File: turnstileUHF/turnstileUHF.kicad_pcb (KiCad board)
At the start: 2 copper layers, 98 x 98 mm, 49 parts, among them Q1 2N7002, Q2 2N7002, Q3 2N7002, Q4 2N7002, Q5 AO3401A, Q6 AO3401A, Q7 AO3401A, Q8 2N7002, SW1 SW_DIP_x04

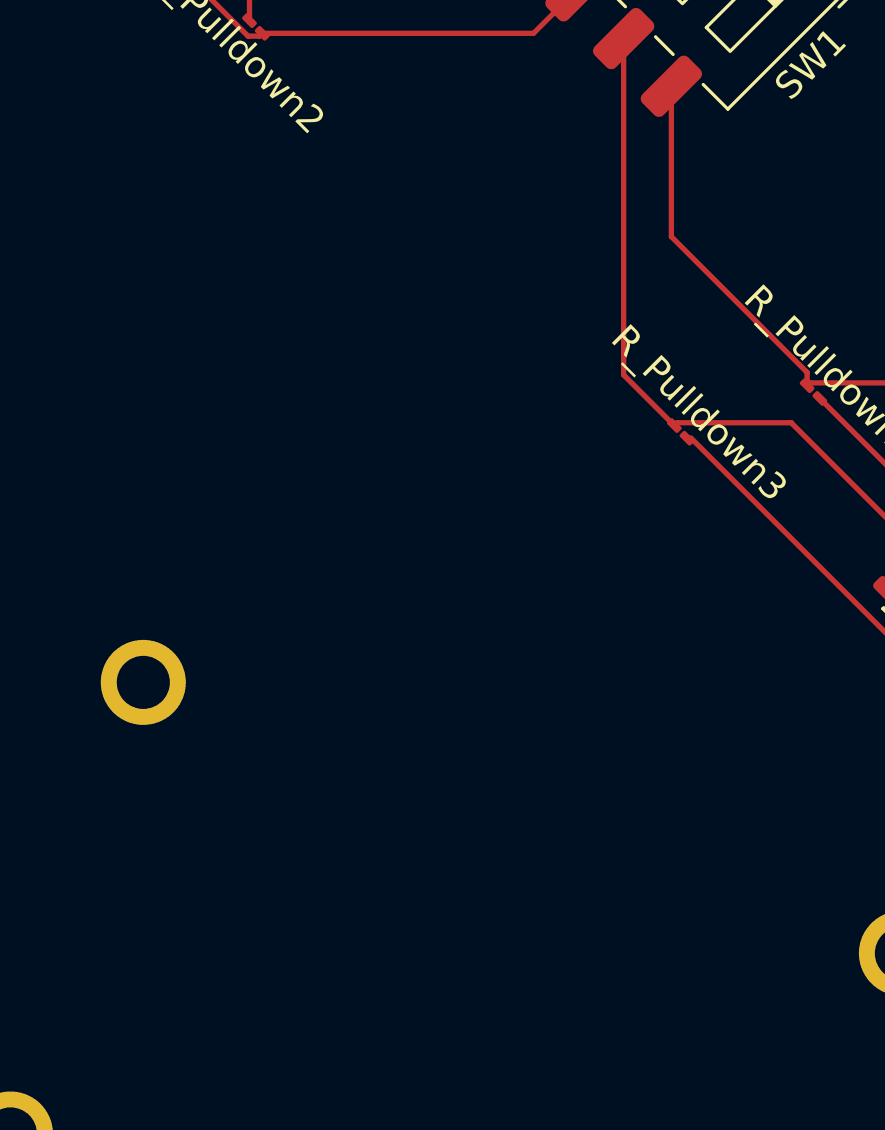
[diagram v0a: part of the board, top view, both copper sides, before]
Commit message: added trace antennas with coax links
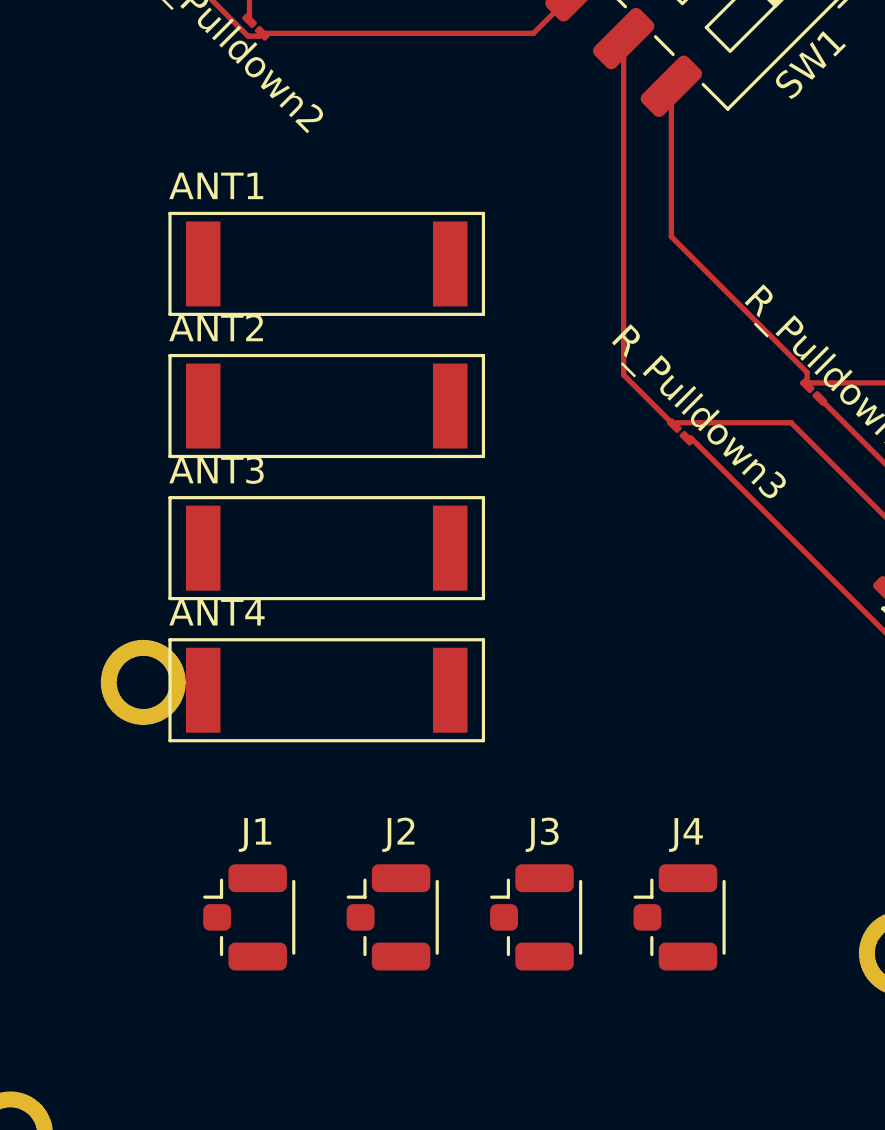
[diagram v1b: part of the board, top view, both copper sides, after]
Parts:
- added ANT1: Antenna, RF_Antenna:Coilcraft_MA5532-AE_RFID, F.Cu at (176.7, 124.4)
- added ANT2: Antenna, RF_Antenna:Coilcraft_MA5532-AE_RFID, F.Cu at (176.7, 129.8)
- added ANT3: Antenna, RF_Antenna:Coilcraft_MA5532-AE_RFID, F.Cu at (176.7, 135.1)
- added ANT4: Antenna, RF_Antenna:Coilcraft_MA5532-AE_RFID, F.Cu at (176.7, 140.5)
- added J1: Conn_Coaxial, Connector_Coaxial:U.FL_Hirose_U.FL-R-SMT-1_Vertical, F.Cu at (174.1, 149.0)
- added J2: Conn_Coaxial, Connector_Coaxial:U.FL_Hirose_U.FL-R-SMT-1_Vertical, F.Cu at (179.5, 149.0)
- added J3: Conn_Coaxial, Connector_Coaxial:U.FL_Hirose_U.FL-R-SMT-1_Vertical, F.Cu at (184.9, 149.0)
- added J4: Conn_Coaxial, Connector_Coaxial:U.FL_Hirose_U.FL-R-SMT-1_Vertical, F.Cu at (190.3, 149.0)

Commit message: Added new 74HCT238D decoder and re-organisation of schematic
Added the 74HCT238D decoder and I also re-organised the schematic.
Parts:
- added U1: 74HCT238D, inspireFly:SOT109-1_NXP, F.Cu at (176.1, 127.4)
- moved ANT4 48.1 mm to (143.2, 106.0)
- moved ANT1 31.8 mm to (146.7, 114.0)
- moved ANT2 31.1 mm to (147.0, 120.5)
- moved ANT3 30.2 mm to (147.5, 127.5)
- moved J4 4.42 mm to (188.5, 145.0)

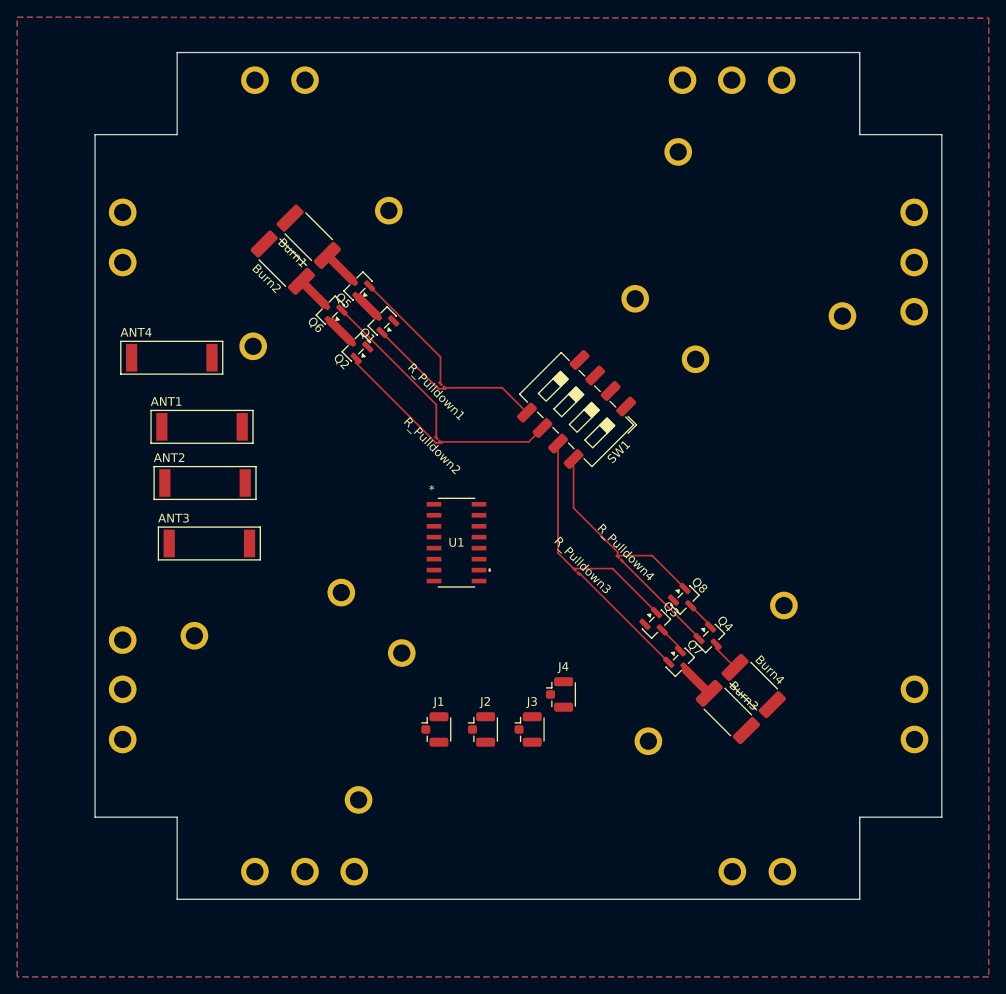
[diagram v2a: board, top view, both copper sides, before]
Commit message: Further changes made. Added SMA connector & Changed the placement of the trace antennas
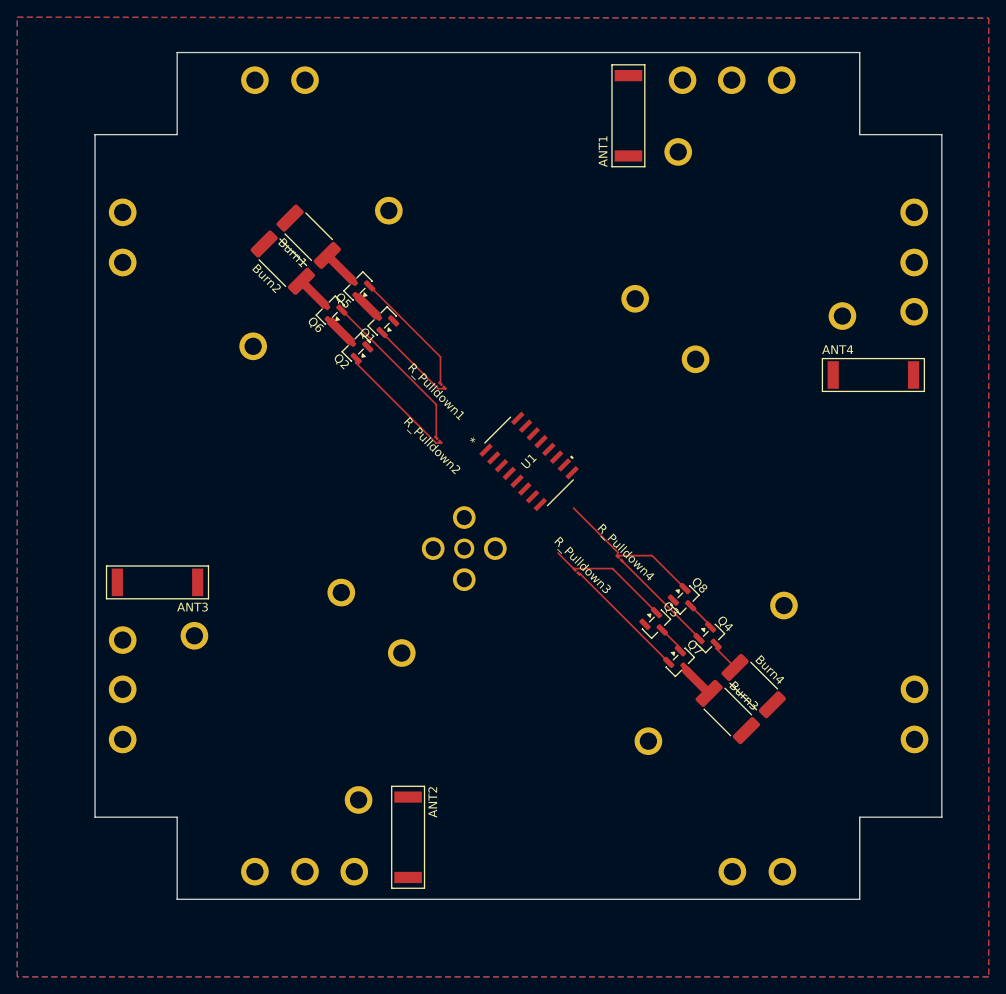
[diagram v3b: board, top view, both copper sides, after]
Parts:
- removed J1, J2, J3, J4: Conn_Coaxial, Connector_Coaxial:U.FL_Hirose_U.FL-R-SMT-1_Vertical
- removed SW1: SW_DIP_x04, Button_Switch_SMD:SW_DIP_SPSTx04_Slide_6.7x11.72mm_W8.61mm_P2.54mm_LowProfile
- added J5: RFPC-SMA28-F, inspireFly:GRADCONN_RFPC-SMA28-F, B.Cu at (177.0, 128.1)
- moved ANT4 81.2 mm to (224.3, 108.0)
- moved ANT1 61.1 mm to (196.0, 78.0), turned to 90 degrees
- moved ANT2 47.3 mm to (170.5, 161.5), turned to -90 degrees
- moved U1 12.6 mm to (184.5, 118.0), turned to 45 degrees
- moved ANT3 7.50 mm to (141.5, 132.0), turned to 180 degrees
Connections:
- ANT2 pad 1: unconnected-(ANT2-~-Pad1) -> Net-(ANT2-~)
- ANT3 pad 1: unconnected-(ANT3-~-Pad1) -> Net-(ANT3-~)
- ANT4 pad 1: unconnected-(ANT4-~-Pad1) -> Net-(ANT4-~)
- Q1 pad 1: Net-(Q1-G) -> FET1
- Q2 pad 1: Net-(Q2-G) -> FET2
- Q3 pad 1: Net-(Q3-G) -> FET3
- Q8 pad 1: Net-(Q8-G) -> FET4
- R_Pulldown1 pad 1: Net-(Q1-G) -> FET1
- R_Pulldown2 pad 1: Net-(Q2-G) -> FET2
- R_Pulldown3 pad 1: Net-(Q3-G) -> FET3
- R_Pulldown4 pad 1: Net-(Q8-G) -> FET4
- U1 pad 1: unconnected-(U1-A0-Pad1) -> GND
- U1 pad 12: unconnected-(U1-Y3-Pad12) -> FET4
- U1 pad 13: unconnected-(U1-Y2-Pad13) -> FET3
- U1 pad 14: unconnected-(U1-Y1-Pad14) -> FET2
- U1 pad 15: unconnected-(U1-Y0-Pad15) -> FET1
- U1 pad 16: unconnected-(U1-VCC-Pad16) -> Supply Voltage - 5V
- U1 pad 2: unconnected-(U1-A1-Pad2) -> GPIO1
- U1 pad 3: unconnected-(U1-A2-Pad3) -> GPIO2
- U1 pad 4: unconnected-(U1-E*1-Pad4) -> GND
- U1 pad 5: unconnected-(U1-E*2-Pad5) -> GND
- U1 pad 6: unconnected-(U1-E3-Pad6) -> Supply Voltage - 5V
- U1 pad 8: unconnected-(U1-GND-Pad8) -> GND
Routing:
- net Net-(Q3-G): track 27.0 -> 0.00 mm
- net Net-(Q2-G): track 26.6 -> 0.00 mm
- net Net-(Q8-G): track 22.8 -> 0.00 mm
- net Net-(Q1-G): track 20.7 -> 0.00 mm
- net FET4: track 0.00 -> 17.1 mm
- net FET3: track 0.00 -> 14.4 mm
- net FET2: track 0.00 -> 14.2 mm
- net FET1: track 0.00 -> 9.97 mm

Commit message: Meeting changes 09-25-2026
Changes made to the schematic, ready to be routed
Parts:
- removed ANT1: Antenna, RF_Antenna:Coilcraft_MA5532-AE_RFID
- moved Burn4 52.0 mm to (210.8, 92.0), turned to 45 degrees
- moved Q4 41.5 mm to (205.2, 97.0), turned to 45 degrees
- moved Q8 34.1 mm to (200.8, 100.0), turned to 45 degrees
- moved ANT4 26.0 mm to (225.3, 134.0)
- moved R_Pulldown4 21.8 mm to (196.0, 107.5), turned to 45 degrees
- moved ANT3 0.50 mm to (141.5, 132.5), turned to 0 degrees
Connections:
- ANT3 pad 1: Net-(ANT3-~) -> Net-(ANT2-~)
- ANT4 pad 1: Net-(ANT4-~) -> Net-(ANT2-~)
- J5 pad 1: unconnected-(J5-Pad1) -> Net-(ANT2-~)
- J5 pad G1: Net-(ANT4-~) -> GND
- J5 pad G2: Net-(ANT3-~) -> GND
- J5 pad G3: Net-(ANT2-~) -> GND
- J5 pad G4: Net-(ANT5-~) -> GND

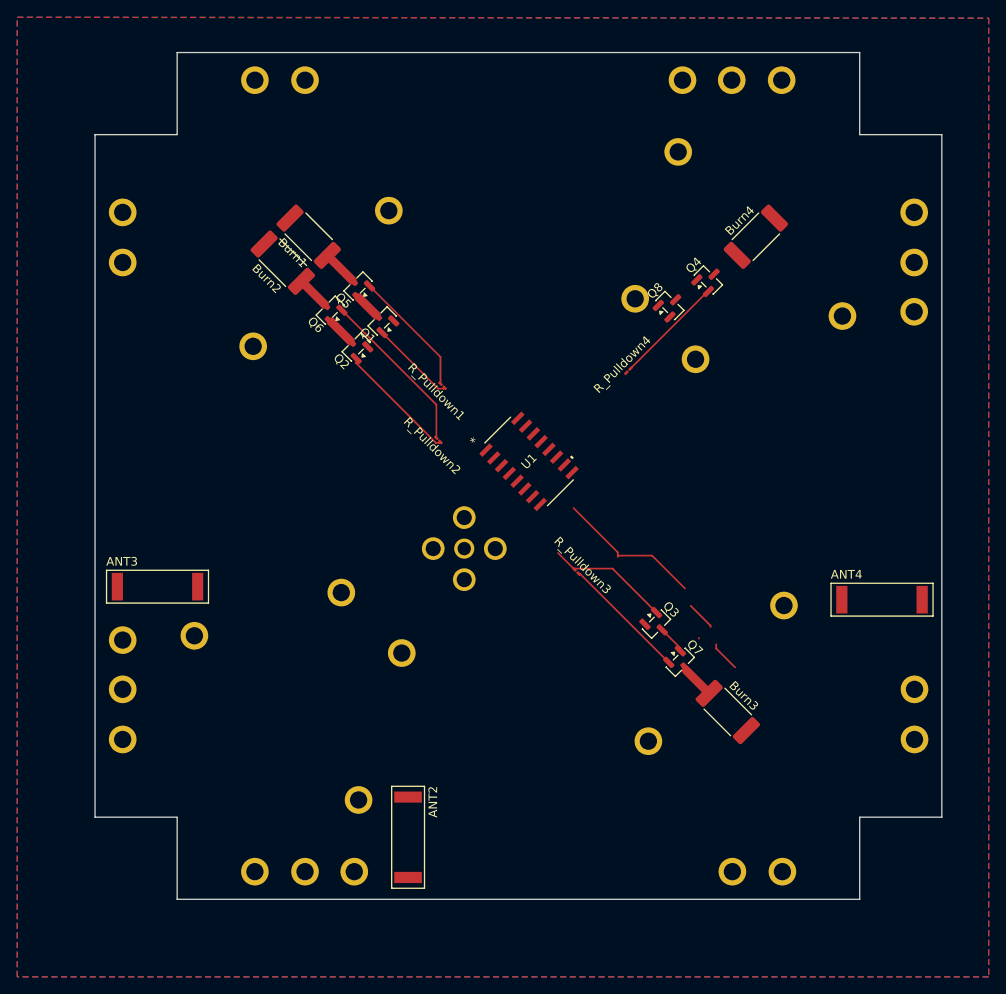
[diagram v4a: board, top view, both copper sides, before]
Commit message: upated burn wire routing
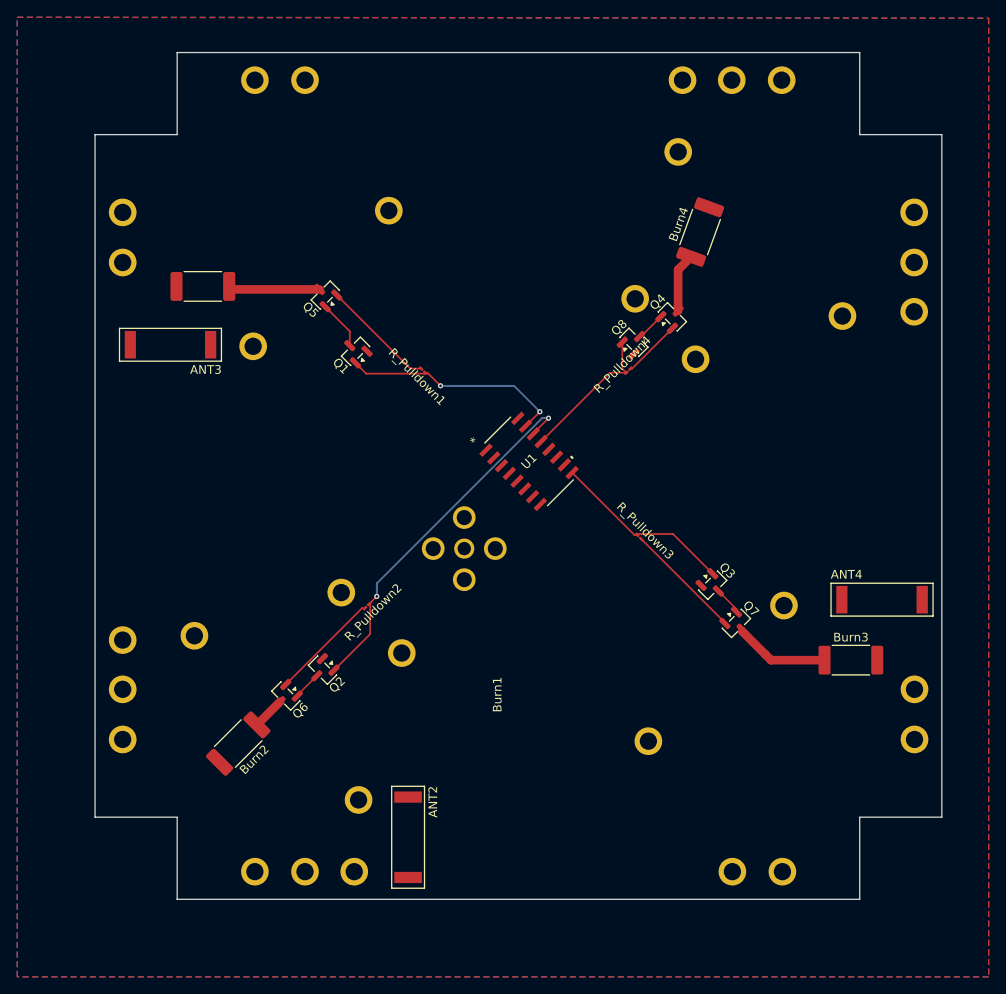
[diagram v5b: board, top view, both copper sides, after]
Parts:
- moved Burn2 55.9 mm to (150.8, 150.7), turned to -135 degrees
- moved Q6 45.0 mm to (156.3, 145.2), turned to -135 degrees
- moved Q2 37.6 mm to (160.6, 142.2), turned to -135 degrees
- moved ANT3 28.0 mm to (143.0, 104.5), turned to 180 degrees
- moved R_Pulldown2 20.9 mm to (165.8, 134.7), turned to -135 degrees
- moved Burn3 15.5 mm to (221.8, 141.0), turned to 0 degrees
- moved Burn1 13.5 mm to (146.8, 97.8), turned to 180 degrees
- moved R_Pulldown3 8.28 mm to (197.2, 126.8)
- moved Q3 7.91 mm to (205.8, 132.3)
- moved Q7 7.91 mm to (208.5, 136.8)
- moved Burn4 6.48 mm to (204.3, 91.5), turned to 70 degrees
- moved Q4 5.96 mm to (201.1, 101.3)
- moved Q8 5.96 mm to (196.6, 104.2)
- moved Q1 4.67 mm to (164.4, 105.3)
- moved Q5 3.93 mm to (160.9, 98.8)
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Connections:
- Q3 pad 1: FET3 -> FET4
- Q8 pad 1: FET4 -> FET3
- R_Pulldown3 pad 1: FET3 -> FET4
- R_Pulldown4 pad 1: FET4 -> FET3
- U1 pad 12: FET4 -> unconnected-(U1-Y3-Pad12)
- U1 pad 9: unconnected-(U1-Y6-Pad9) -> FET4
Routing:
- net FET2: track 14.2 -> 42.7 mm, vias 0 -> 2
- net FET1: track 9.97 -> 26.1 mm, vias 0 -> 2
- net Net-(Q7-D): track 4.04 -> 10.9 mm
- net Net-(Q5-D): track 4.08 -> 10.6 mm
- net Net-(Q6-S): track 19.3 -> 12.8 mm
- net Net-(Q4-S): track 12.7 -> 6.79 mm
- net FET4: track 17.1 -> 21.2 mm
- net Net-(Q4-D): track 3.58 -> 6.90 mm
- net Net-(Q1-D): track 2.99 -> 5.68 mm
- net FET3: track 14.4 -> 16.9 mm
- net Net-(Q5-S): track 14.7 -> 13.3 mm
- net Net-(Q7-S): track 14.7 -> 13.8 mm
